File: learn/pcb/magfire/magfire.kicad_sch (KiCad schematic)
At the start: 3 parts, among them J1 Conn_01x07_Pin, J2 Conn_01x07_Pin, U1 74HC14

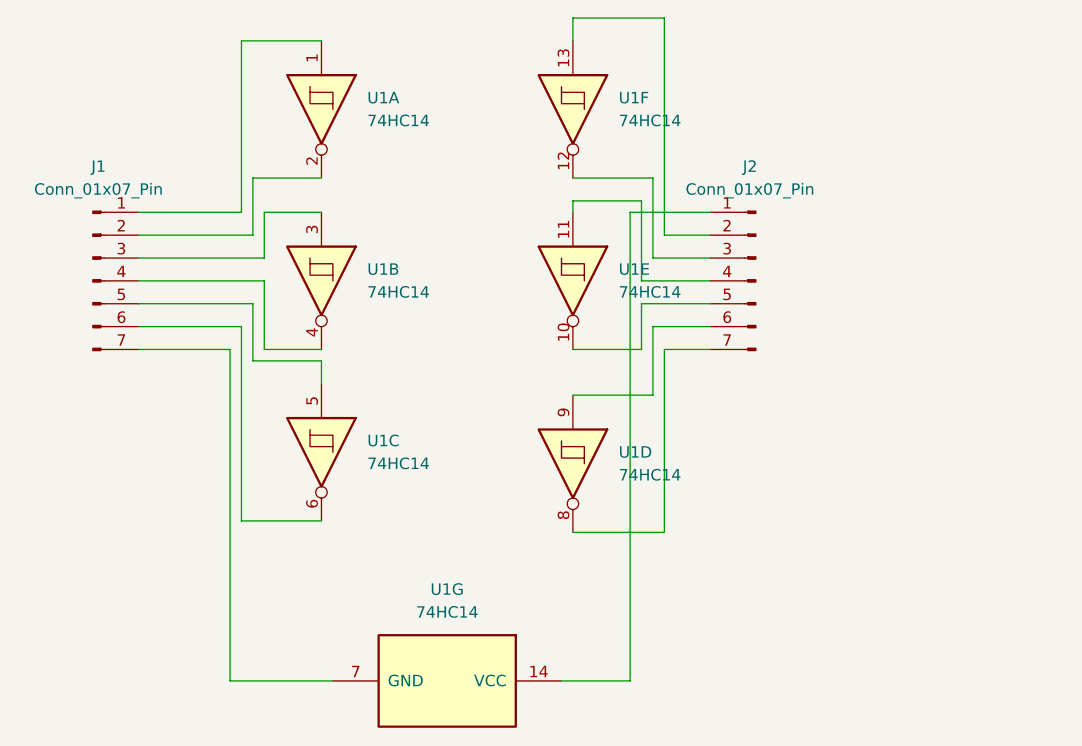
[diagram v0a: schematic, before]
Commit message: add image and update BOM
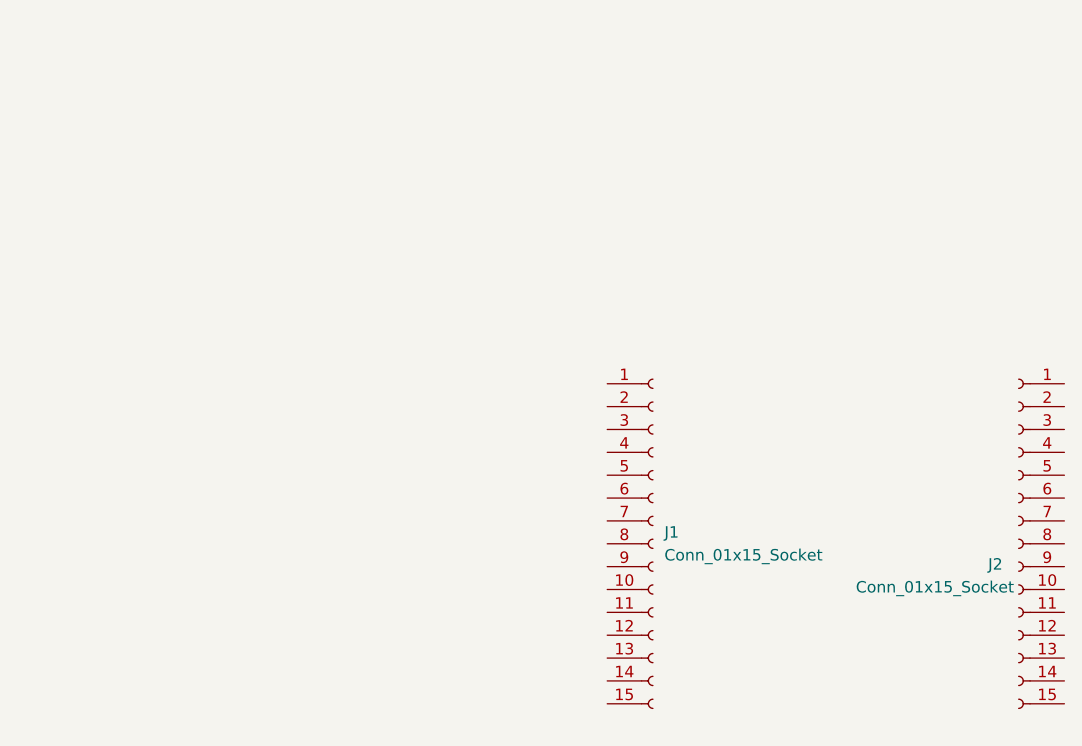
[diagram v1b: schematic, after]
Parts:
- removed J1, J2: Conn_01x07_Pin, Connector_PinHeader_2.54mm:PinHeader_1x07_P2.54mm_Vertical, symbol Connector:Conn_01x07_Pin
- removed U1: 74HC14, Package_SO:TSSOP-14_4.4x5mm_P0.65mm, symbol 74xx:74HC14
- added J1, J2: Conn_01x15_Socket, symbol Connector:Conn_01x15_Socket
